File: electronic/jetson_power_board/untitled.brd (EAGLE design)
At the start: 59.4 x 29.2 mm, 20 parts

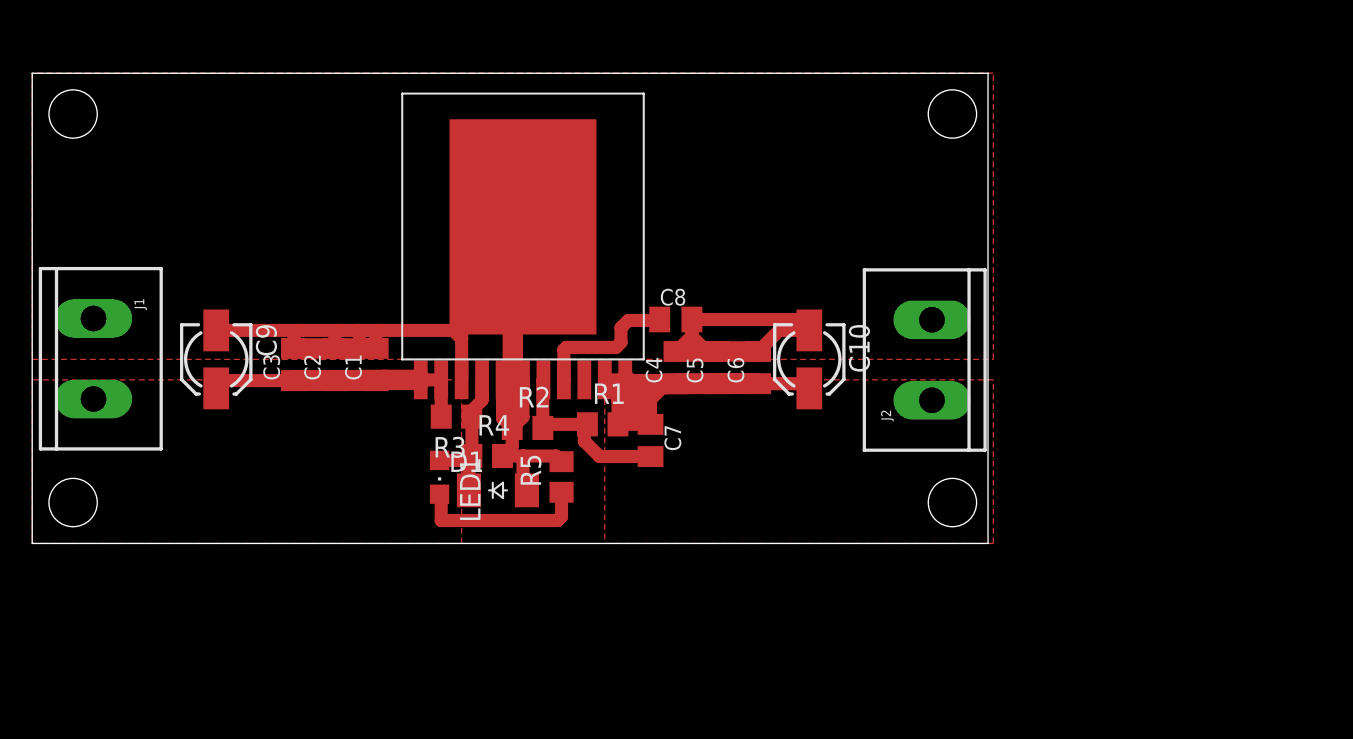
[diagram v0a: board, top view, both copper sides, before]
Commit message: add sim models
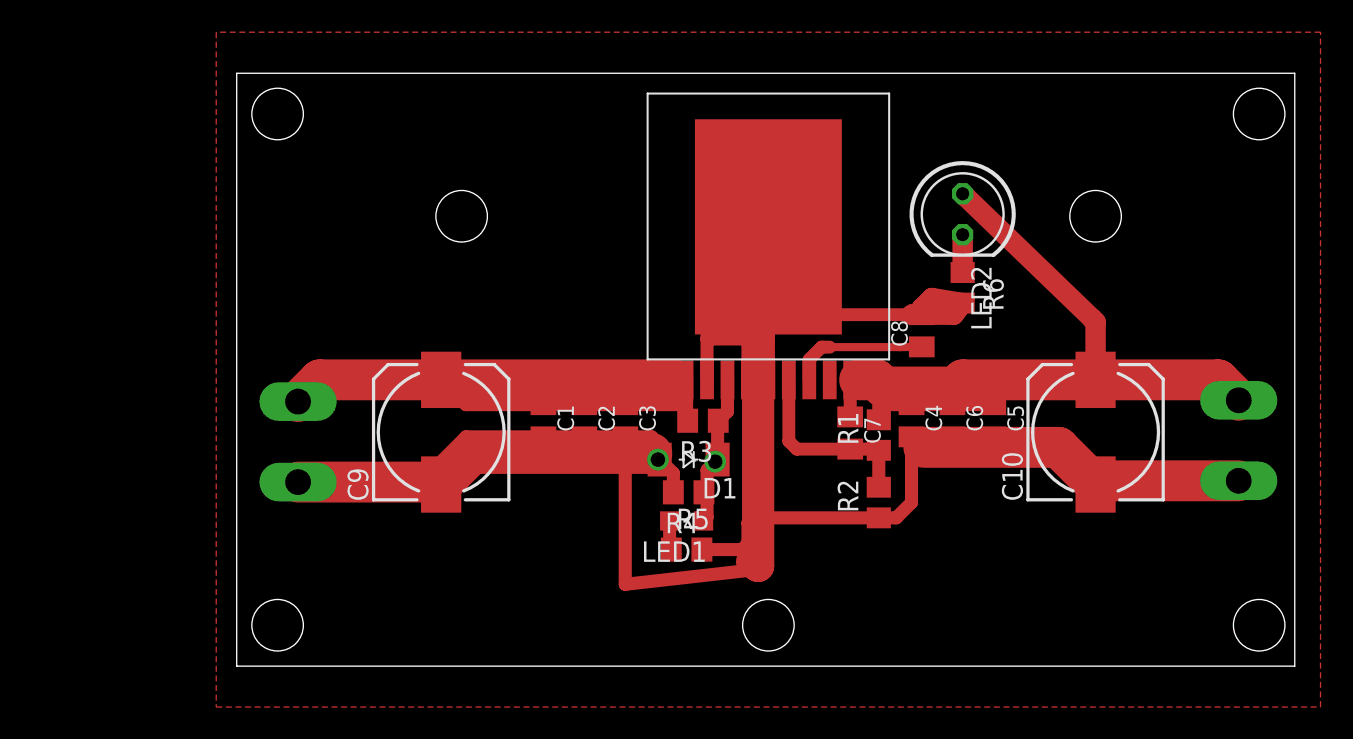
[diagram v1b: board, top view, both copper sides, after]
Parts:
- added LED2: (no value), led:LED5MM
- added R6: (no value), resistor:R0805
- C10, C9: device resistor:153CLV-0405 -> resistor:153CLV-0810
- moved R2 22.3 mm to (39.9, 2.54), turned to 90 degrees
- moved C3 20.9 mm to (24.1, 7.62), turned to 270 degrees
- moved J2 19.0 mm to (62.2, 8.89), flipped to the bottom, turned to 270 degrees
- moved C10 18.3 mm to (53.3, 6.91), turned to 90 degrees
- moved C5 17.5 mm to (47.0, 7.62), turned to 270 degrees
- moved R1 17.2 mm to (39.9, 6.73), turned to 90 degrees
- moved J1 16.3 mm to (3.81, 3.81), flipped to the bottom, turned to 90 degrees
- moved C2 15.9 mm to (21.6, 7.62), turned to 270 degrees
- moved LED1 15.6 mm to (27.9, 1.40), turned to 90 degrees
- moved R3 15.3 mm to (29.0, 7.62)
- moved C8 15.3 mm to (42.5, 13.2), turned to 90 degrees
- moved U$1 15.2 mm to (33.0, 10.2)
- moved C4 15.0 mm to (41.9, 7.62), turned to 270 degrees
- moved C9 14.7 mm to (12.7, 6.91), turned to 90 degrees
- moved R4 12.7 mm to (28.1, 3.17), turned to 180 degrees
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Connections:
- new net N$5: LED2.K, R6.1
- net GND: now also R6.2
- net VDD: now also LED2.A
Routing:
- net GND: track 89.2 -> 172.5 mm, vias 0 -> 1
- net V+: track 21.5 -> 50.1 mm
- net VDD: track 33.8 -> 53.0 mm
- net N$4: track 10.8 -> 1.82 mm
- net N$5: track 0.00 -> 2.35 mm
- net N$1: track 9.14 -> 8.57 mm
- net N$3: track 9.33 -> 9.65 mm, vias 0 -> 1
- removed copper zone on layer 1, net V+
- removed copper zone on layer 1, net VDD
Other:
- board size 59.4 x 29.2 mm -> 65.7 x 36.8 mm

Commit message: some model changes
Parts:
- removed D1: CGRM4004-G, diode:SOD-123_MINI-SMA
- removed LED1: (no value), led:CHIPLED_0805
- removed LED2: (no value), led:LED5MM
- removed R3, R4, R5, R6: (no value), resistor:R0805
- added C11: (no value), resistor:153CLV-0810
- added J3: (no value), SparkFun-Connectors:SCREWTERMINAL-5MM-2
- added U1: (no value), SparkFun-IC-Power:SOT223
- moved J2 3.81 mm to (62.2, 5.08)
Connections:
- removed net N$3: D1.C, LED1.A, R3.1, R4.1, U$1.EN
- removed net N$4: LED1.C, R5.1
- net GND: now also C11.-, J3.2, U1.1; no longer D1.A, R4.2, R5.2, R6.2
- net N$5: now also C11.+, J3.1, U1.2, U1.4; no longer LED2.K, R6.1
- net V+: no longer R3.2
- net VDD: now also U1.3; no longer LED2.A
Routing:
- net GND: track 172.5 -> 144.7 mm, vias 1 -> 0
- net N$5: track 2.35 -> 20.4 mm
- net VDD: track 53.0 -> 43.1 mm
- net N$3: track 9.65 -> 0.00 mm, vias 1 -> 0
- net N$4: track 1.82 -> 0.00 mm
- net V+: track 50.1 -> 48.9 mm
